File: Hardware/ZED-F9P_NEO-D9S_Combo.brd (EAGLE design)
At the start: 43.2 x 63.5 mm, 174 parts, among them J1 ANTENNA-SMA-GROUNDEDEDGE_SMA, J2 Qwiic Right Angle, J3 USB Female Type C Connector, J4 Qwiic Right Angle, J6 USB Female Type C Connector, U1 U-BLOX_NEO-D9S-00B, U2 3.3V, U3 POWER-DIVIDER, U4 U-BLOX_ZED-F9P

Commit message: Add IC-16658 GNSS Power Divider. Delete New_parts.lbr
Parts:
- U3: device New_Parts:PD0922J5050S2HF_ANA -> SparkFun-GPS:PD0922J5050S2HF_ANA
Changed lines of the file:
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@@
 <layers>
 <layer number="1" name="Top" color="4" fill="1" visible="yes" active="yes"/>
-<layer number="2" name="Route2" color="63" fill="3" visible="yes" active="yes"/>
-<layer number="15" name="Route15" color="23" fill="6" visible="yes" active="yes"/>
+<layer number="2" name="Route2" color="63" fill="3" visible="no" active="yes"/>
+<layer number="15" name="Route15" color="23" fill="6" visible="no" active="yes"/>
 <layer number="16" name="Bottom" color="1" fill="1" visible="yes" active="yes"/>
 <layer number="17" name="Pads" color="2" fill="1" visible="yes" active="yes"/>
@@
 <layer number="27" name="tValues" color="7" fill="1" visible="no" active="yes"/>
 <layer number="28" name="bValues" color="7" fill="1" visible="no" active="yes"/>
-<layer number="29" name="tStop" color="7" fill="3" visible="yes" active="yes"/>
-<layer number="30" name="bStop" color="7" fill="6" visible="yes" active="yes"/>
+<layer number="29" name="tStop" color="7" fill="3" visible="no" active="yes"/>
+<layer number="30" name="bStop" color="7" fill="6" visible="no" active="yes"/>
 <layer number="31" name="tCream" color="7" fill="4" visible="no" active="yes"/>
 <layer number="32" name="bCream" color="7" fill="5" visible="no" active="yes"/>
@@
 <layer number="37" name="tTest" color="7" fill="1" visible="no" active="yes"/>
 <layer number="38" name="bTest" color="7" fill="1" visible="no" active="yes"/>
-<layer number="39" name="tKeepout" color="4" fill="11" visible="yes" active="yes"/>
-<layer number="40" name="bKeepout" color="1" fill="11" visible="yes" active="yes"/>
+<layer number="39" name="tKeepout" color="4" fill="11" visible="no" active="yes"/>
+<layer number="40" name="bKeepout" color="1" fill="11" visible="no" active="yes"/>
 <layer number="41" name="tRestrict" color="4" fill="10" visible="no" active="yes"/>
 <layer number="42" name="bRestrict" color="1" fill="10" visible="no" active="yes"/>
@@
 <layer number="49" name="Reference" color="13" fill="1" visible="no" active="yes"/>
 <layer number="50" name="dxf" color="7" fill="1" visible="no" active="yes"/>
-<layer number="51" name="tDocu" color="6" fill="1" visible="no" active="yes"/>
+<layer number="51" name="tDocu" color="6" fill="1" visible="yes" active="yes"/>
 <layer number="52" name="bDocu" color="7" fill="1" visible="no" active="yes"/>
 <layer number="91" name="Nets" color="2" fill="1" visible="no" active="no"/>
@@
 </element>
 <element name="LOGO5" library="SparkFun-Aesthetics" package="ORDERING_INSTRUCTIONS" value="SPECIAL_INSTRUCTIONS-ORDERING" x="54.61" y="63.5" smashed="yes"/>
-<element name="U3" library="New_Parts" package="PD0922J5050S2HF_ANA" value="POWER-DIVIDER" x="26.67" y="31.75" smashed="yes" rot="R270">
-<attribute name="DIGI-KEY_PART_NUMBER_1" value="1173-1094-2-ND" x="26.67" y="31.75" size="1.778" layer="27" ratio="15" rot="R270" display="off"/>
+<element name="U3" library="SparkFun-GPS" package="PD0922J5050S2HF_ANA" value="POWER-DIVIDER" x="26.67" y="31.75" smashed="yes" rot="R270">
 <attribute name="MANUFACTURER_PART_NUMBER" value="PD0922J5050S2HF" x="26.67" y="31.75" size="1.778" layer="27" ratio="15" rot="R270" display="off"/>
 <attribute name="NAME" x="27.686" y="32.893" size="0.508" layer="25" ratio="6" rot="SR270"/>
-<attribute name="PROD_ID" value="IC-16689" x="26.67" y="31.75" size="1.778" layer="27" ratio="15" rot="R270" display="off"/>
+<attribute name="PROD_ID" value="IC-16658" x="26.67" y="31.75" size="1.778" layer="27" ratio="15" rot="R270" display="off"/>
 <attribute name="VALUE" x="25.019" y="33.02" size="0.508" layer="27" ratio="6" rot="SR270"/>
 </element>

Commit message: Use RF Library copy of IC-16658
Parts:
- U3: device SparkFun-GPS:PD0922J5050S2HF_ANA -> SparkFun-RF:PD0922J5050S2HF_ANA
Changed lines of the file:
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@@
 <layers>
 <layer number="1" name="Top" color="4" fill="1" visible="yes" active="yes"/>
-<layer number="2" name="Route2" color="63" fill="3" visible="no" active="yes"/>
-<layer number="15" name="Route15" color="23" fill="6" visible="no" active="yes"/>
+<layer number="2" name="Route2" color="63" fill="3" visible="yes" active="yes"/>
+<layer number="15" name="Route15" color="23" fill="6" visible="yes" active="yes"/>
 <layer number="16" name="Bottom" color="1" fill="1" visible="yes" active="yes"/>
 <layer number="17" name="Pads" color="2" fill="1" visible="yes" active="yes"/>
@@
 <layer number="23" name="tOrigins" color="15" fill="1" visible="yes" active="yes"/>
 <layer number="24" name="bOrigins" color="15" fill="1" visible="yes" active="yes"/>
-<layer number="25" name="tNames" color="7" fill="1" visible="no" active="yes"/>
-<layer number="26" name="bNames" color="7" fill="1" visible="no" active="yes"/>
-<layer number="27" name="tValues" color="7" fill="1" visible="no" active="yes"/>
-<layer number="28" name="bValues" color="7" fill="1" visible="no" active="yes"/>
-<layer number="29" name="tStop" color="7" fill="3" visible="no" active="yes"/>
-<layer number="30" name="bStop" color="7" fill="6" visible="no" active="yes"/>
-<layer number="31" name="tCream" color="7" fill="4" visible="no" active="yes"/>
-<layer number="32" name="bCream" color="7" fill="5" visible="no" active="yes"/>
-<layer number="33" name="tFinish" color="6" fill="3" visible="no" active="yes"/>
-<layer number="34" name="bFinish" color="6" fill="6" visible="no" active="yes"/>
-<layer number="35" name="tGlue" color="7" fill="4" visible="no" active="yes"/>
-<layer number="36" name="bGlue" color="7" fill="5" visible="no" active="yes"/>
-<layer number="37" name="tTest" color="7" fill="1" visible="no" active="yes"/>
-<layer number="38" name="bTest" color="7" fill="1" visible="no" active="yes"/>
-<layer number="39" name="tKeepout" color="4" fill="11" visible="no" active="yes"/>
-<layer number="40" name="bKeepout" color="1" fill="11" visible="no" active="yes"/>
-<layer number="41" name="tRestrict" color="4" fill="10" visible="no" active="yes"/>
-<layer number="42" name="bRestrict" color="1" fill="10" visible="no" active="yes"/>
-<layer number="43" name="vRestrict" color="2" fill="10" visible="no" active="yes"/>
-<layer number="44" name="Drills" color="7" fill="1" visible="no" active="yes"/>
+<layer number="25" name="tNames" color="7" fill="1" visible="yes" active="yes"/>
+<layer number="26" name="bNames" color="7" fill="1" visible="yes" active="yes"/>
+<layer number="27" name="tValues" color="7" fill="1" visible="yes" active="yes"/>
+<layer number="28" name="bValues" color="7" fill="1" visible="yes" active="yes"/>
+<layer number="29" name="tStop" color="7" fill="3" visible="yes" active="yes"/>
+<layer number="30" name="bStop" color="7" fill="6" visible="yes" active="yes"/>
+<layer number="31" name="tCream" color="7" fill="4" visible="yes" active="yes"/>
+<layer number="32" name="bCream" color="7" fill="5" visible="yes" active="yes"/>
+<layer number="33" name="tFinish" color="6" fill="3" visible="yes" active="yes"/>
+<layer number="34" name="bFinish" color="6" fill="6" visible="yes" active="yes"/>
+<layer number="35" name="tGlue" color="7" fill="4" visible="yes" active="yes"/>
+<layer number="36" name="bGlue" color="7" fill="5" visible="yes" active="yes"/>
+<layer number="37" name="tTest" color="7" fill="1" visible="yes" active="yes"/>
+<layer number="38" name="bTest" color="7" fill="1" visible="yes" active="yes"/>
+<layer number="39" name="tKeepout" color="4" fill="11" visible="yes" active="yes"/>
+<layer number="40" name="bKeepout" color="1" fill="11" visible="yes" active="yes"/>
+<layer number="41" name="tRestrict" color="4" fill="10" visible="yes" active="yes"/>
+<layer number="42" name="bRestrict" color="1" fill="10" visible="yes" active="yes"/>
+<layer number="43" name="vRestrict" color="2" fill="10" visible="yes" active="yes"/>
+<layer number="44" name="Drills" color="7" fill="1" visible="yes" active="yes"/>
 <layer number="45" name="Holes" color="7" fill="1" visible="yes" active="yes"/>
-<layer number="46" name="Milling" color="3" fill="1" visible="no" active="yes"/>
-<layer number="47" name="Measures" color="7" fill="1" visible="no" active="yes"/>
-<layer number="48" name="Document" color="7" fill="1" visible="no" active="yes"/>
-<layer number="49" name="Reference" color="13" fill="1" visible="no" active="yes"/>
-<layer number="50" name="dxf" color="7" fill="1" visible="no" active="yes"/>
+<layer number="46" name="Milling" color="3" fill="1" visible="yes" active="yes"/>
+<layer number="47" name="Measures" color="7" fill="1" visible="yes" active="yes"/>
+<layer number="48" name="Document" color="7" fill="1" visible="yes" active="yes"/>
+<layer number="49" name="Reference" color="13" fill="1" visible="yes" active="yes"/>
+<layer number="50" name="dxf" color="7" fill="1" visible="yes" active="yes"/>
 <layer number="51" name="tDocu" color="6" fill="1" visible="yes" active="yes"/>
-<layer number="52" name="bDocu" color="7" fill="1" visible="no" active="yes"/>
+<layer number="52" name="bDocu" color="7" fill="1" visible="yes" active="yes"/>
 <layer number="91" name="Nets" color="2" fill="1" visible="no" active="no"/>
 <layer number="92" name="Busses" color="1" fill="1" visible="no" active="no"/>
@@
 </element>
 <element name="LOGO5" library="SparkFun-Aesthetics" package="ORDERING_INSTRUCTIONS" value="SPECIAL_INSTRUCTIONS-ORDERING" x="54.61" y="63.5" smashed="yes"/>
-<element name="U3" library="SparkFun-GPS" package="PD0922J5050S2HF_ANA" value="POWER-DIVIDER" x="26.67" y="31.75" smashed="yes" rot="R270">
+<element name="U3" library="SparkFun-RF" package="PD0922J5050S2HF_ANA" value="POWER-DIVIDER" x="26.67" y="31.75" smashed="yes" rot="R270">
+<attribute name="DIGI-KEY_PART_NUMBER_1" value="1173-1094-2-ND" x="26.67" y="31.75" size="1.778" layer="27" rot="R270" display="off"/>
 <attribute name="MANUFACTURER_PART_NUMBER" value="PD0922J5050S2HF" x="26.67" y="31.75" size="1.778" layer="27" ratio="15" rot="R270" display="off"/>
 <attribute name="NAME" x="27.686" y="32.893" size="0.508" layer="25" ratio="6" rot="SR270"/>

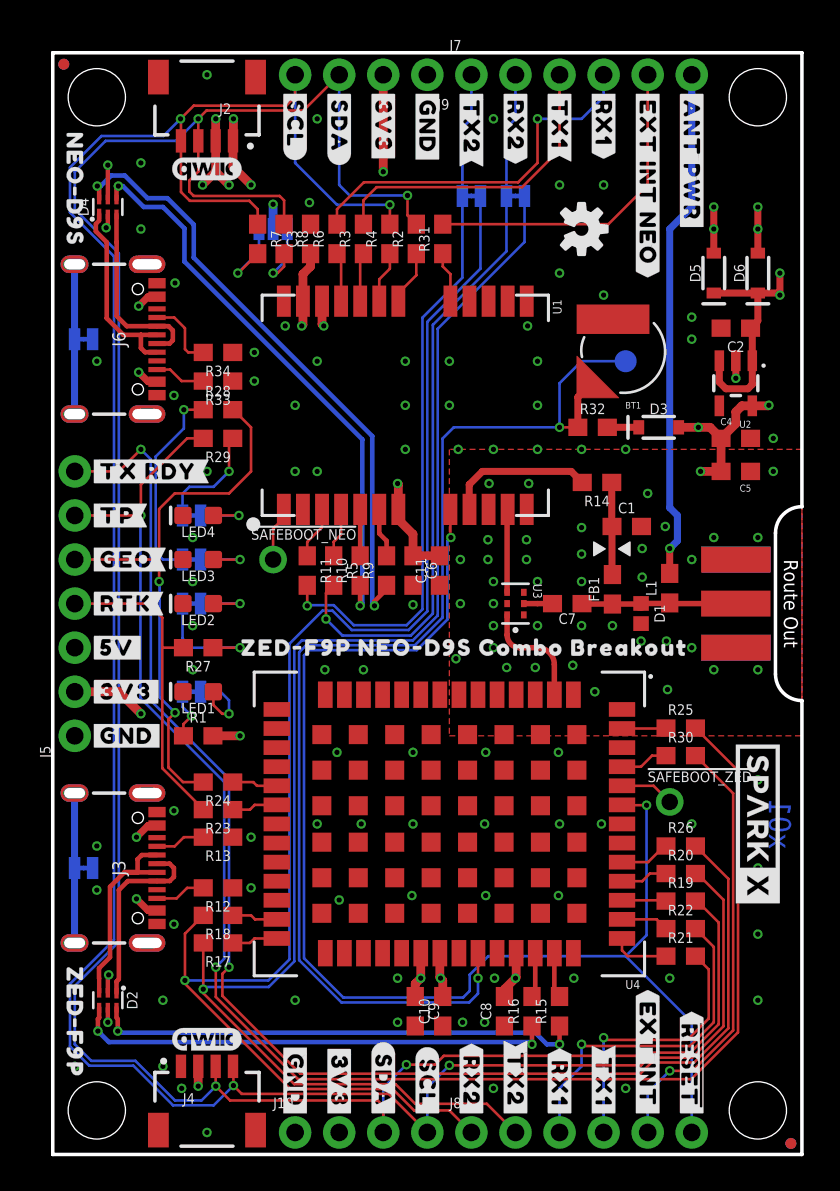
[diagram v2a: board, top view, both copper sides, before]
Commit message: x02 PCB - inverts RTK LED
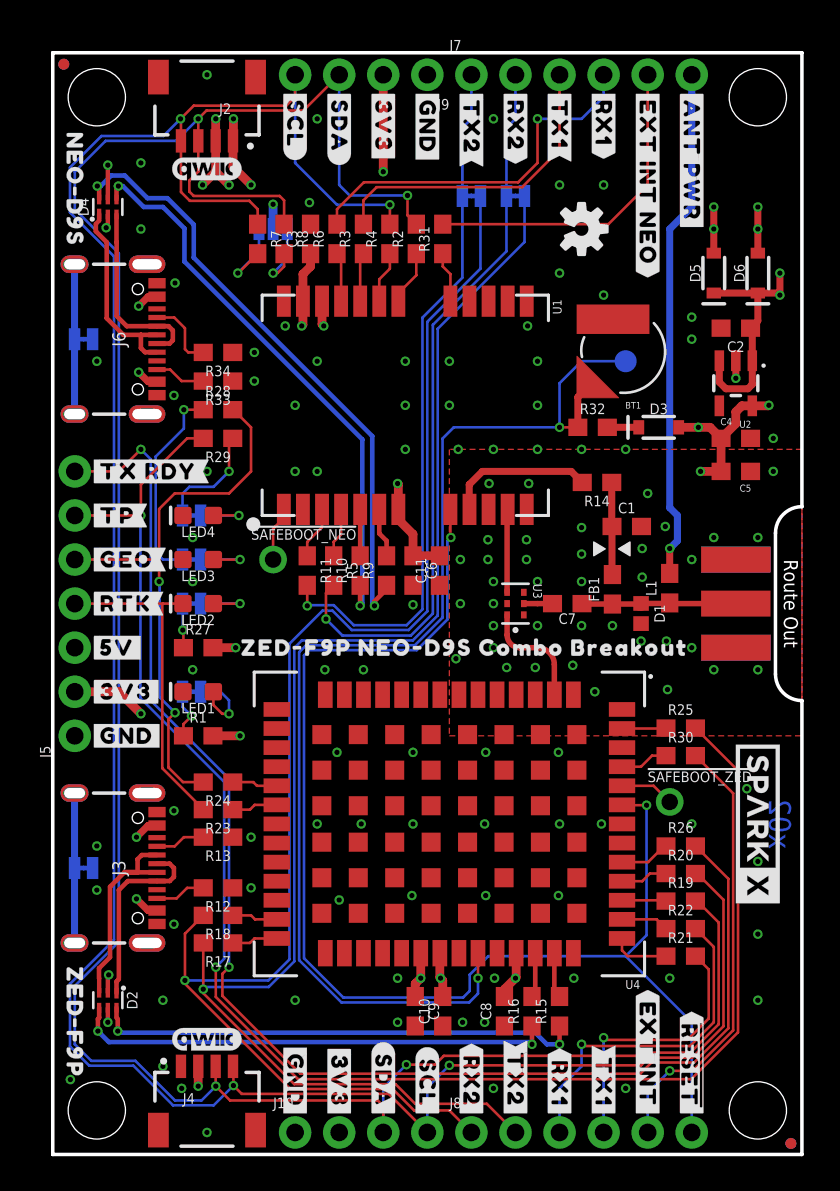
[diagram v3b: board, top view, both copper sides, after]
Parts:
- turned R27 to 0 degrees
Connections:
- net 3.3V: now also R27.2
- net GND: no longer LED2.C
- net RTK: now also LED2.C; no longer R27.2
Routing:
- net N$28: track 7.11 -> 2.56 mm
- net 3.3V: track 49.0 -> 50.3 mm, vias 17 -> 18
- net GND: vias 127 -> 126
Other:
- board text added: "x02"
- board text removed: "x01"
